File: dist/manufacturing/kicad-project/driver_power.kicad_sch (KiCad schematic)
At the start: 11 parts, among them U34 LMR36510ADDAR

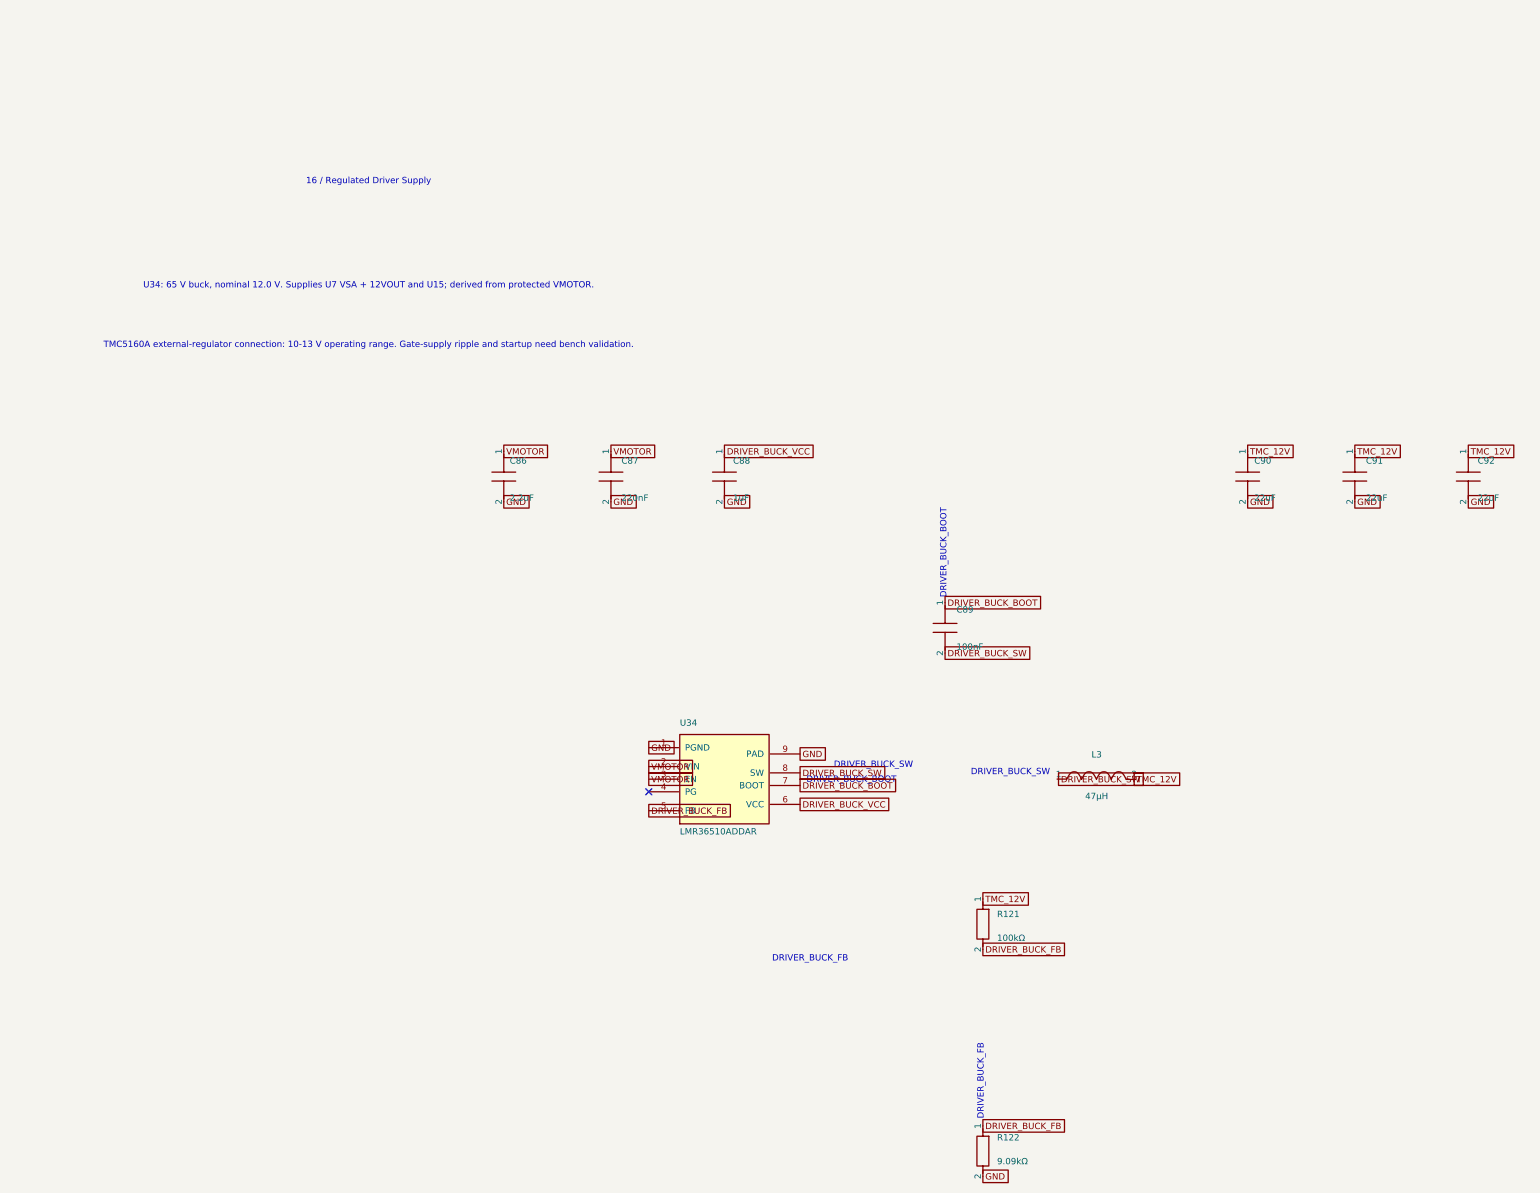
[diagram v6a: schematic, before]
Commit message: Fix source warnings and organize schematic on A4 sheets
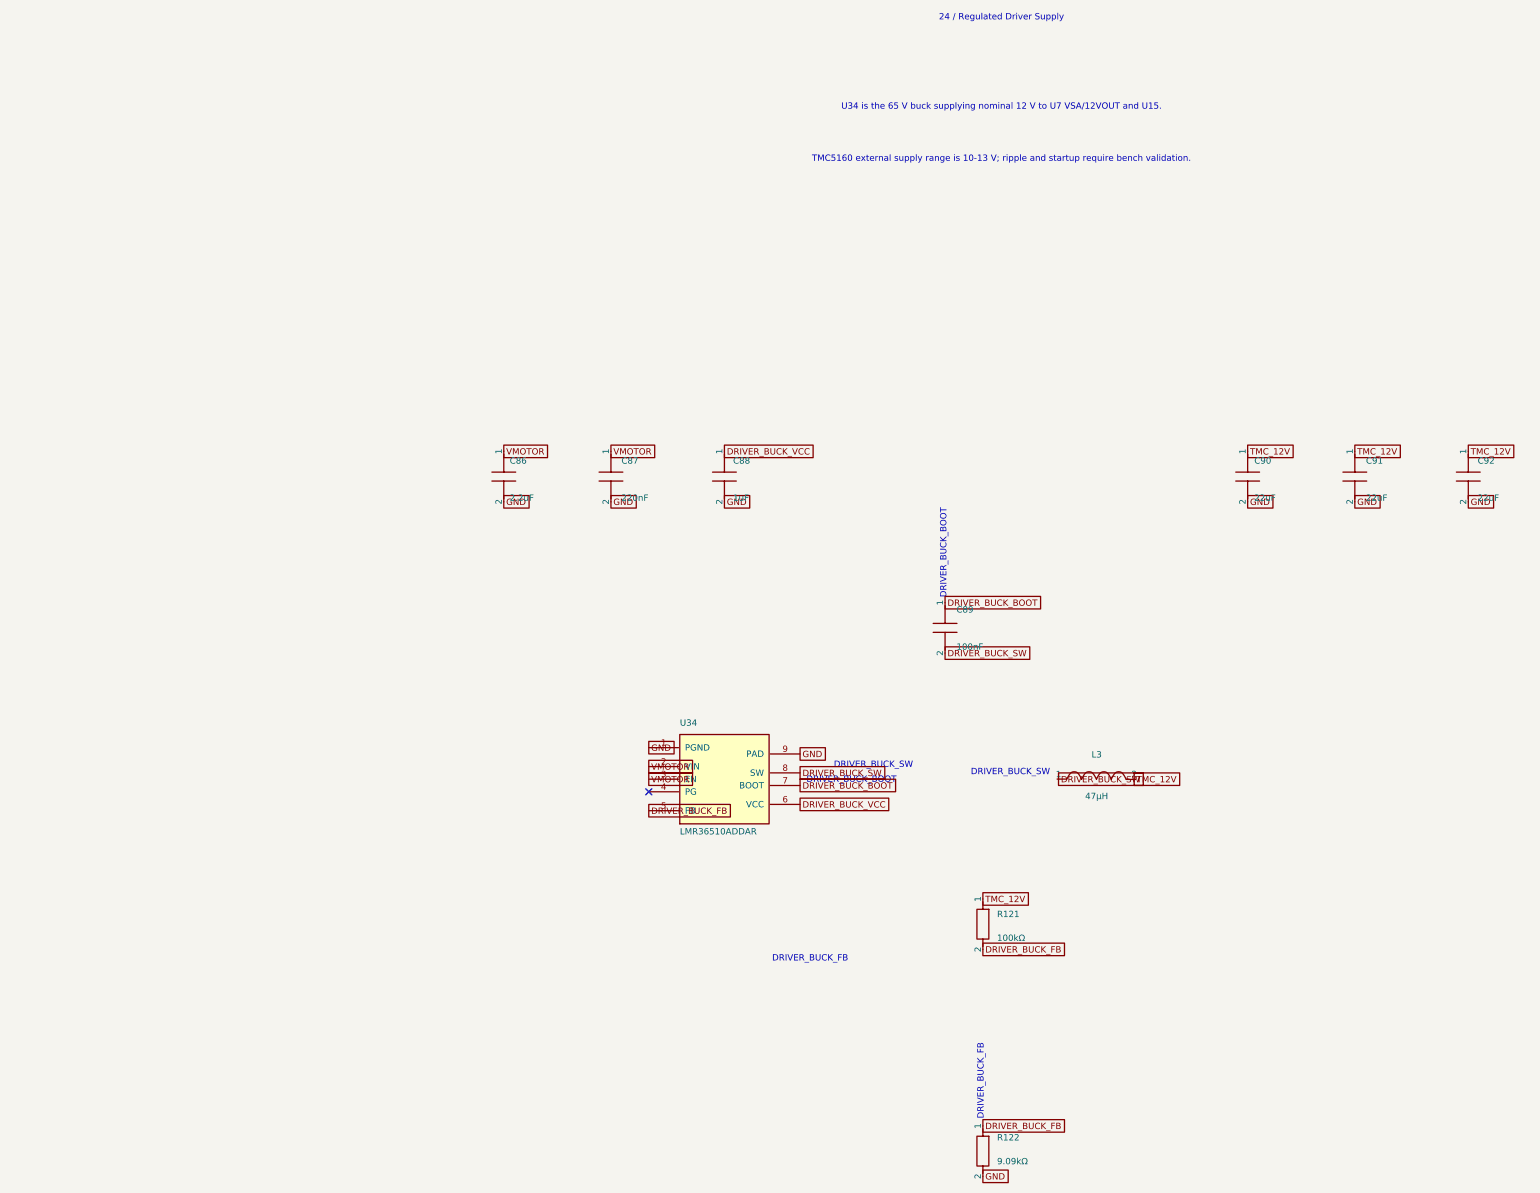
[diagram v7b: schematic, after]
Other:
- note added: "24 / Regulated Driver Supply"
- note added: "TMC5160 external supply range is 10-13 V; ripple and startup require bench validation."
- note added: "U34 is the 65 V buck supplying nominal 12 V to U7 VSA/12VOUT and U15."
- note removed: "16 / Regulated Driver Supply"
- note removed: "TMC5160A external-regulator connection: 10-13 V operating range. Gate-supply ripple and startup need bench validation."
- note removed: "U34: 65 V buck, nominal 12.0 V. Supplies U7 VSA + 12VOUT and U15; derived from protected VMOTOR."
